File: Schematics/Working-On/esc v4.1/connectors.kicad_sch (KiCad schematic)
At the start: 17 parts, among them J1 AVR-ISP-10, J2 Conn_01x04, J3 74651174R, J4 74651174R, J5 74651174R, J6 74651174R, J7 74651174R, U1 TLV76750DRVx

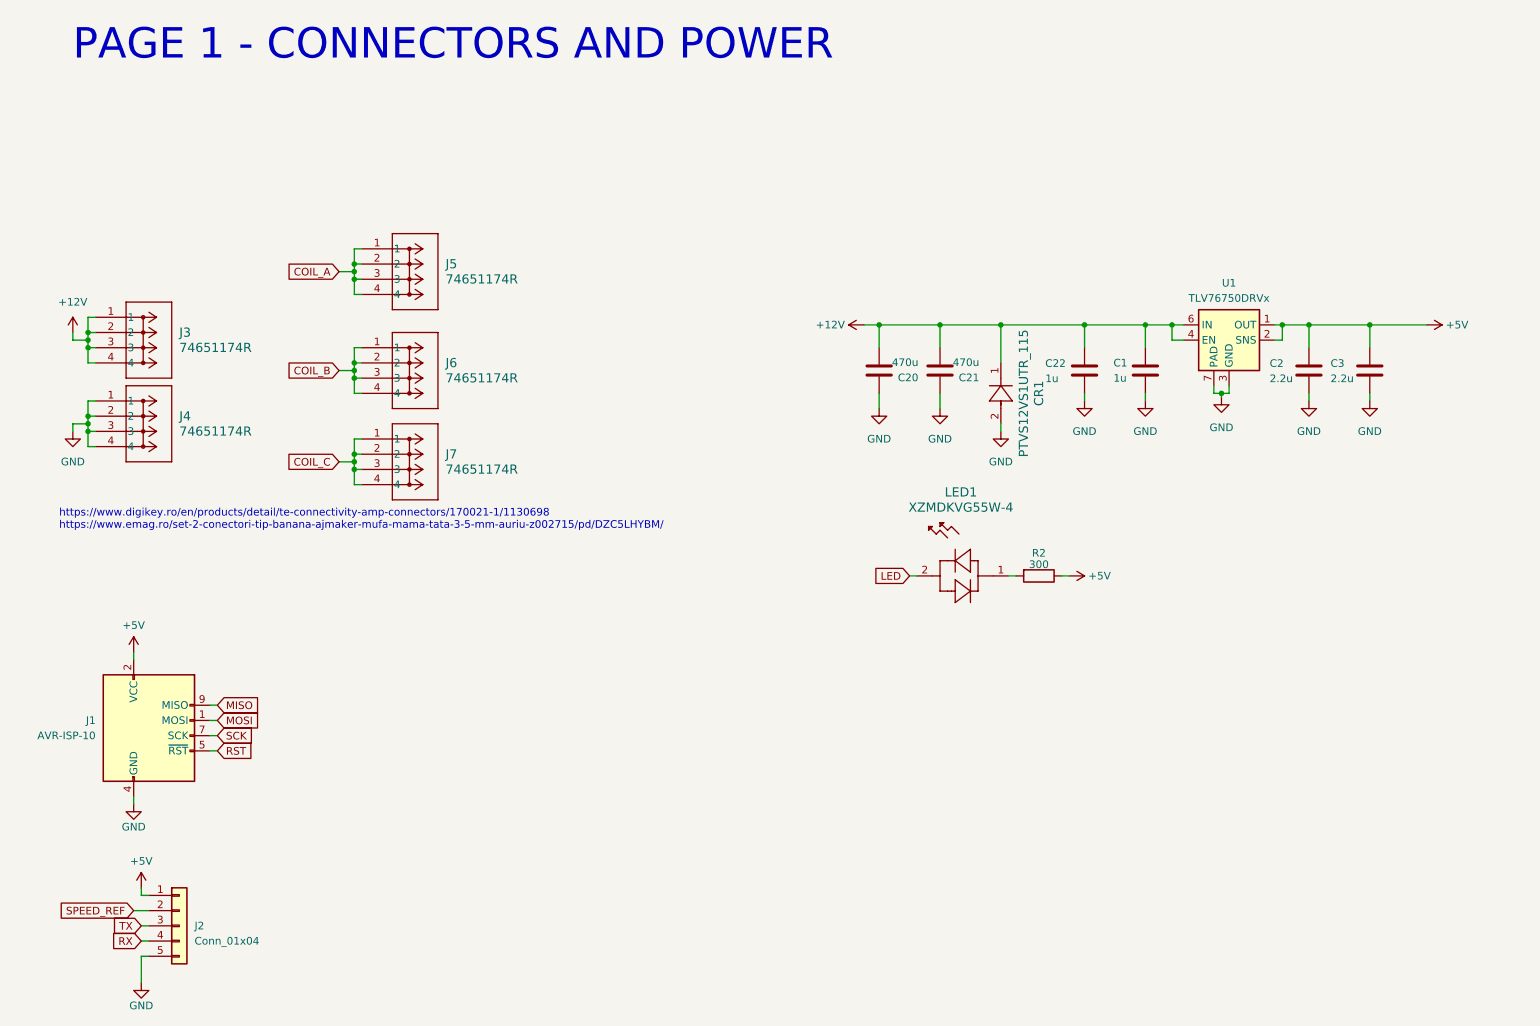
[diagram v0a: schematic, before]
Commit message: New connectors, and BEMF Filter.
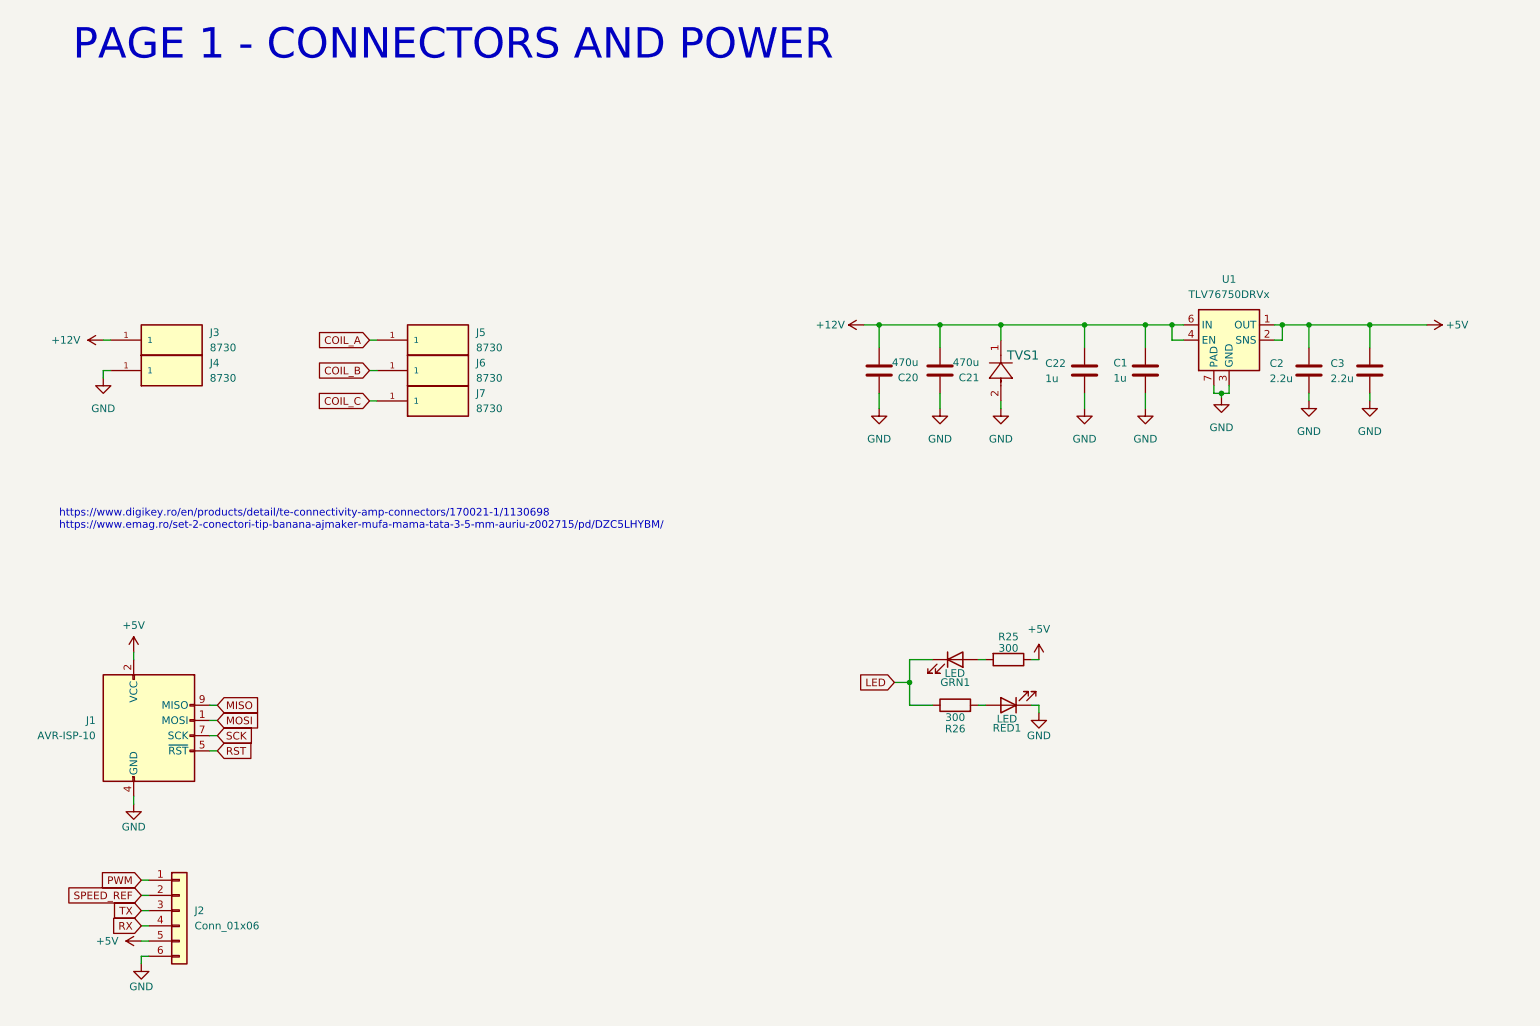
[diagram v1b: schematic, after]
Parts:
- removed J2: Conn_01x04, Connector_PinHeader_2.54mm:PinHeader_1x05_P2.54mm_Vertical, symbol Connector_Generic:Conn_01x05
- removed J3, J4, J5, J6, J7: 74651174R, 74651174:CONN4_74651174R_WRE, symbol 74651174:74651174R
- removed LED1: XZMDKVG55W-4, XZMDKVG55W-4:LED_KVG55W-4_SLD, symbol XZMDKVG55W-4:XZMDKVG55W-4
- removed R2: 300, Resistor_SMD:R_0402_1005Metric, symbol Device:R
- added GRN1, RED1: LED, LED_SMD:LED_0603_1608Metric, symbol Device:LED
- added J2: Conn_01x06, Connector_PinHeader_2.54mm:PinHeader_1x06_P2.54mm_Vertical, symbol Connector_Generic:Conn_01x06
- added J3, J4, J5, J6, J7: 8730, 8730:8730, symbol 8730:8730
- added R25, R26: 300, Resistor_SMD:R_0402_1005Metric, symbol Device:R
- U1: footprint Package_SON:WSON-6-1EP_2x2mm_P0.65mm_EP1x1.6mm_ThermalVias -> TLV76750DRVR:SON65P200X200X80-7N
- renumbered CR1 to TVS1
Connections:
- net +12V: now also J3.1
- net +5V: now also J2.5 (Pin_5), R25.1
- net COIL_A: now also J5.1
- net COIL_B: now also J6.1
- net COIL_C: now also J7.1
- net GND: now also J2.6 (Pin_6), J4.1, RED1.1 (K)
- net LED: now also GRN1.1 (K), R26.1
- net RX: now also J2.4 (Pin_4)
- net SPEED_REF: now also J2.2 (Pin_2)
- net TX: now also J2.3 (Pin_3)
- new net: GRN1.2 (A), R25.2
- new net: R26.2, RED1.2 (A)
- new net PWM: J2.1 (Pin_1)
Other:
- moved on the sheet: TVS1

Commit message: swaped PWM_IN & Comp_Ref_Out, vias finished
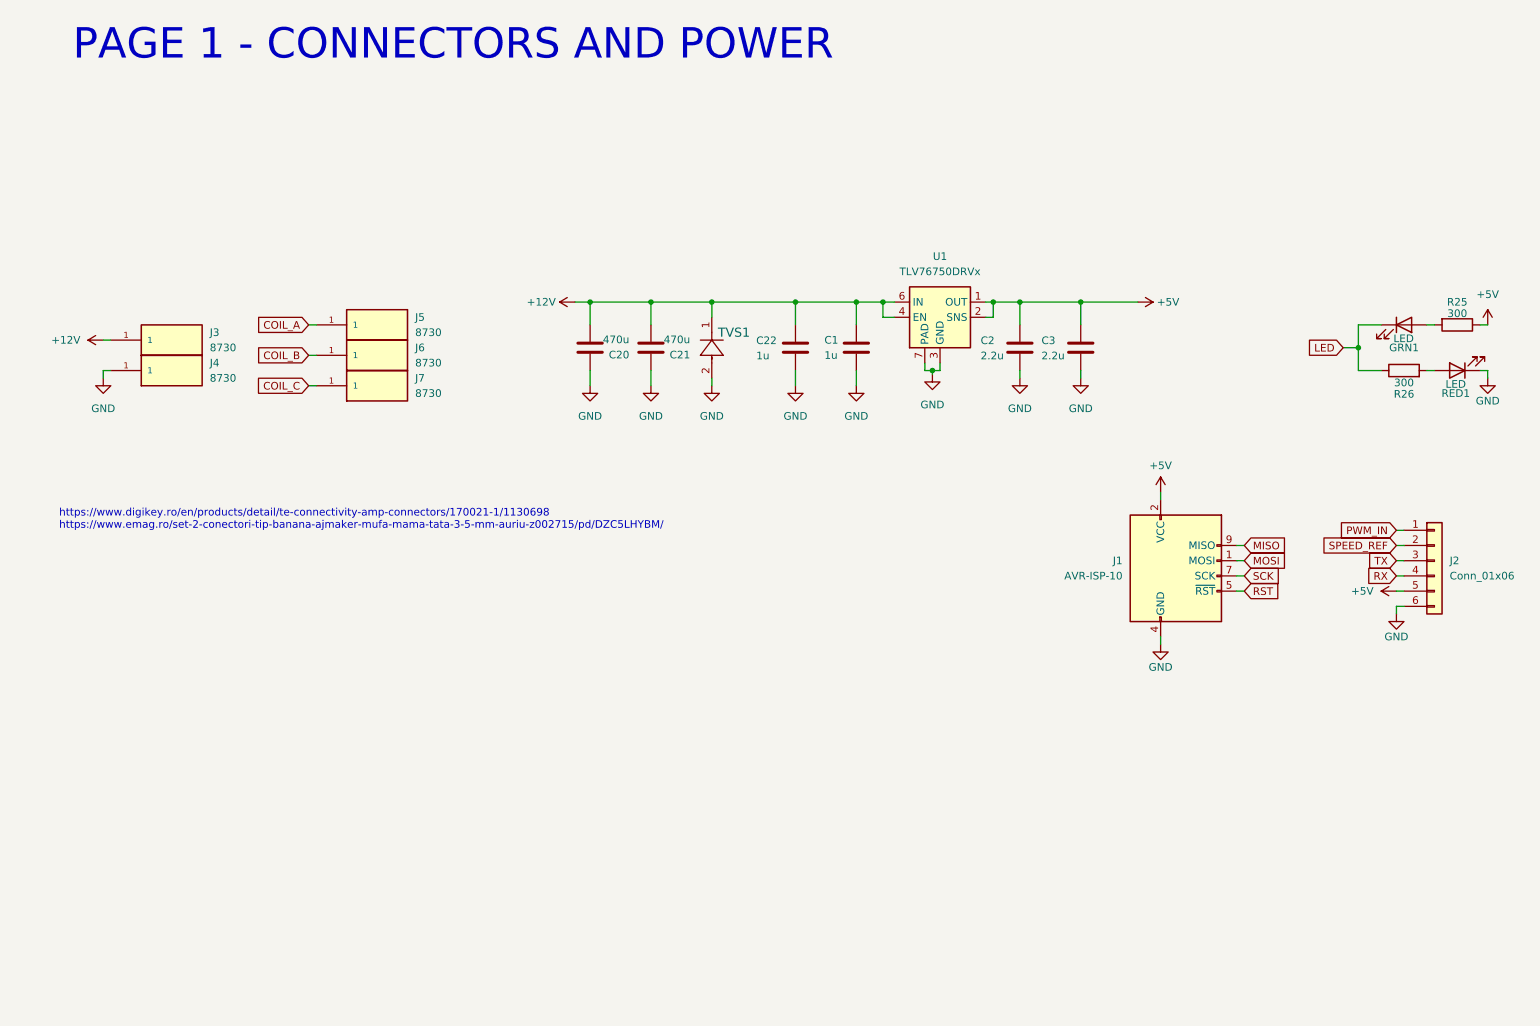
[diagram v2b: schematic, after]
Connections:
- net PWM renamed PWM_IN
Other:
- moved on the sheet: C1, C2, C20, C21, C22, C3, GRN1, J1, J2, J5, J6, J7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

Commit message: Added pins for the BACK-EMFs and PWM Control signals
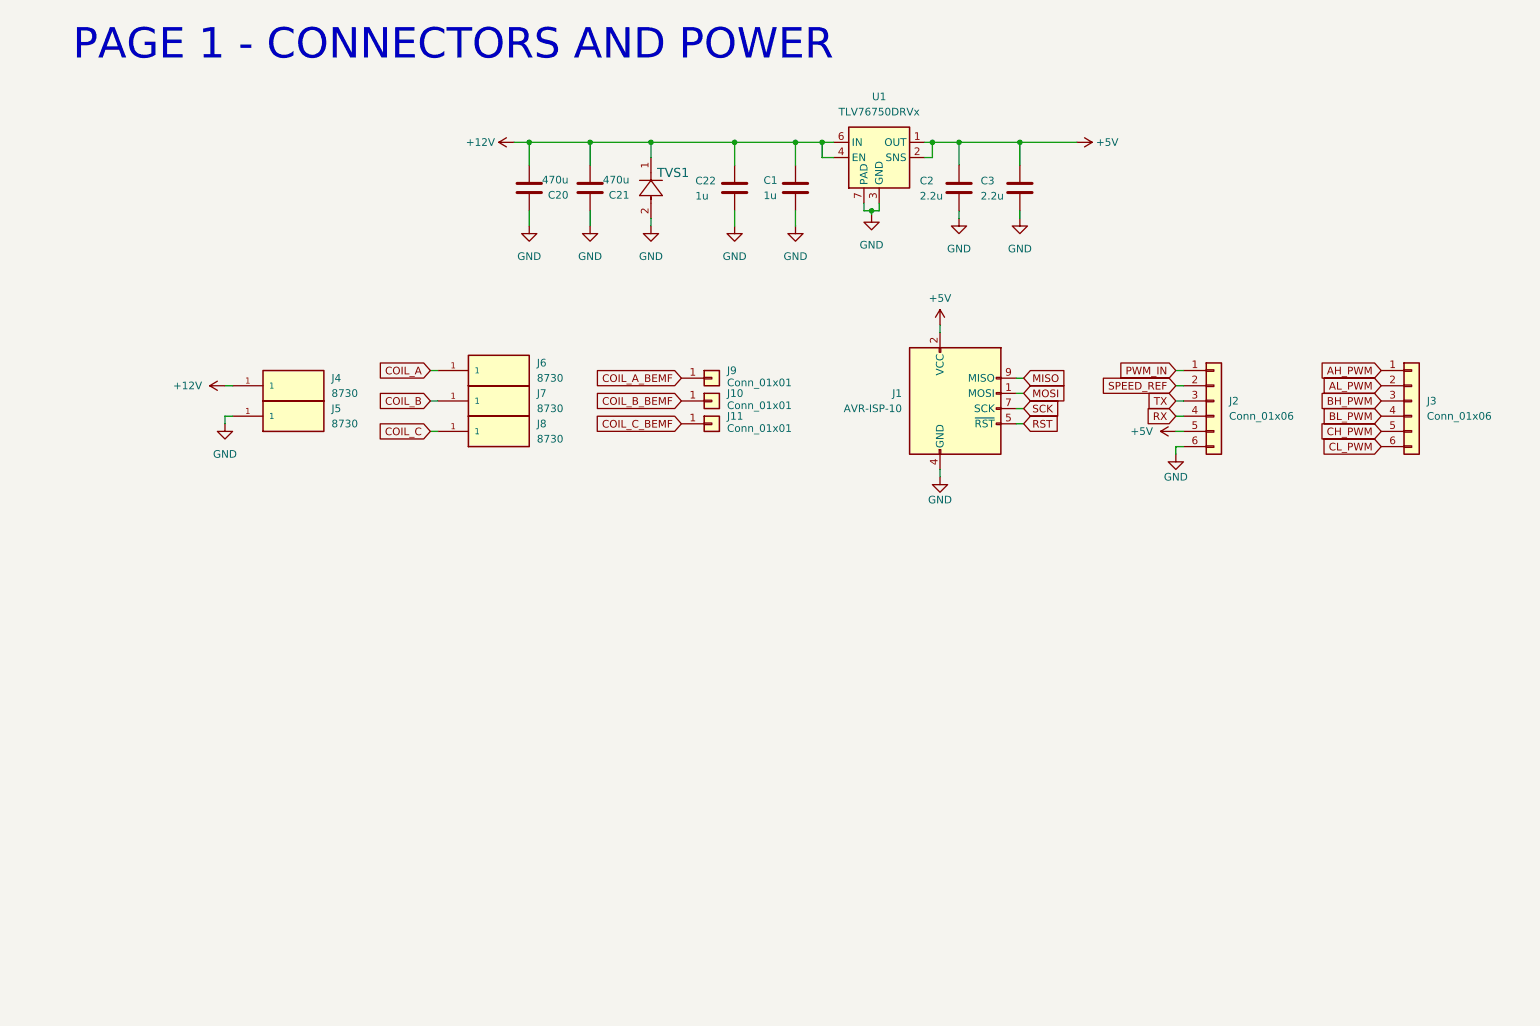
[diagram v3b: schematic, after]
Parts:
- removed GRN1, RED1: LED, LED_SMD:LED_0603_1608Metric, symbol Device:LED
- removed R25, R26: 300, Resistor_SMD:R_0402_1005Metric, symbol Device:R
- added J10, J11, J9: Conn_01x01, Connector_PinHeader_1.00mm:PinHeader_1x01_P1.00mm_Vertical, symbol Connector_Generic:Conn_01x01
- added J3: Conn_01x06, Connector_PinHeader_2.54mm:PinHeader_1x06_P2.54mm_Vertical, symbol Connector_Generic:Conn_01x06
- renumbered J3 to J4, J4 to J5, J5 to J6, J6 to J7, J7 to J8
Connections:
- new net AH_PWM: J3.1 (Pin_1)
- new net AL_PWM: J3.2 (Pin_2)
- new net BH_PWM: J3.3 (Pin_3)
- new net BL_PWM: J3.4 (Pin_4)
- new net CH_PWM: J3.5 (Pin_5)
- new net CL_PWM: J3.6 (Pin_6)
- new net COIL_A_BEMF: J9.1 (Pin_1)
- new net COIL_B_BEMF: J10.1 (Pin_1)
- new net COIL_C_BEMF: J11.1 (Pin_1)
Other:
- note removed: "https://www.digikey.ro/en/products/detail/te-connectivity-amp-connectors/170021-1/1130698 https://www.emag.ro/set-2-conectori-tip-banana-ajmaker-mufa-mama-tata-3-5-mm-auriu-z002715/pd/DZC5LHYBM/"
- moved on the sheet: C1, C2, C20, C21, C22, C3, J1, J2, J4, J5, J6, J7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

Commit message: Ready to order(?)
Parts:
- renumbered C20 to C1, C21 to C2, C22 to C3, C1 to C4, C2 to C5, C3 to C6, J4 to J1, J1 to J10, J2 to J11, J5 to J2, J6 to J3, J7 to J4, J8 to J5, J9 to J6, J10 to J7, J11 to J8, J3 to J9
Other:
- moved on the sheet: J10, J11, J9

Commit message: Ready to order.
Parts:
- J6, J7, J8: footprint Connector_PinHeader_1.00mm:PinHeader_1x01_P1.00mm_Vertical -> Connector_PinHeader_2.54mm:PinHeader_1x01_P2.54mm_Vertical
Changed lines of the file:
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@@
 			)
 		)
-		(property "Footprint" "Connector_PinHeader_1.00mm:PinHeader_1x01_P1.00mm_Vertical"
+		(property "Footprint" "Connector_PinHeader_2.54mm:PinHeader_1x01_P2.54mm_Vertical"
 			(at 130.81 82.55 0)
 			(effects
@@
 			)
 		)
-		(property "Footprint" "Connector_PinHeader_1.00mm:PinHeader_1x01_P1.00mm_Vertical"
+		(property "Footprint" "Connector_PinHeader_2.54mm:PinHeader_1x01_P2.54mm_Vertical"
 			(at 130.81 86.36 0)
 			(effects
@@
 			)
 		)
-		(property "Footprint" "Connector_PinHeader_1.00mm:PinHeader_1x01_P1.00mm_Vertical"
+		(property "Footprint" "Connector_PinHeader_2.54mm:PinHeader_1x01_P2.54mm_Vertical"
 			(at 130.81 78.74 0)
 			(effects
